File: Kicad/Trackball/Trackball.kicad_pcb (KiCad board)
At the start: 2 copper layers, 305.8 x 154.1 mm, 67 parts, among them J1 Battery, J10 Female, J11 Conn_01x04_Female, J12 Conn_01x04_Female, J13 Female, J14 Conn_01x04_Female, J15 Conn_01x04_Female, J17 Conn_01x04_Female, J18 Conn_01x03_Pin, J19 Conn_01x03_Pin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

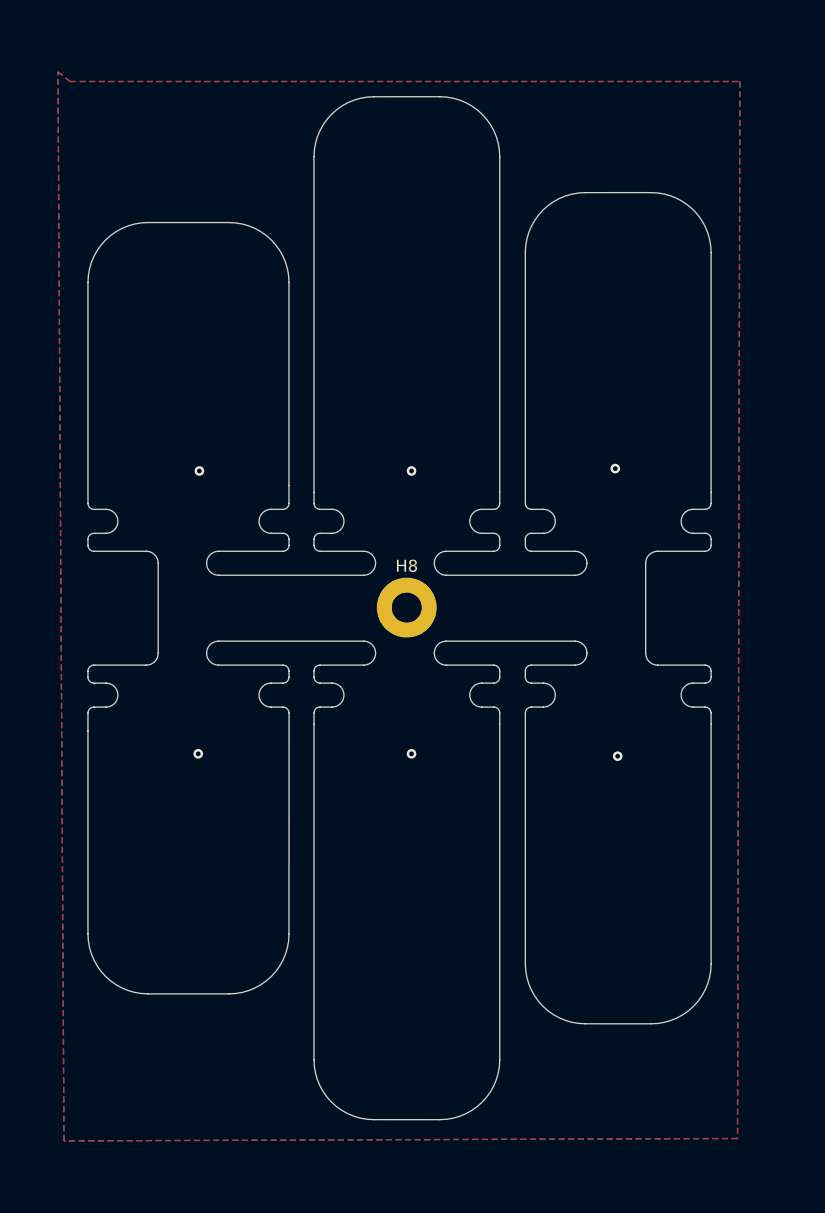
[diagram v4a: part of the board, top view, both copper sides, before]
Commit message: B5: Modified the flaps plate - changed their length as per user feedback. Updated Gerbers for that plate, ordered that plate 20251024.
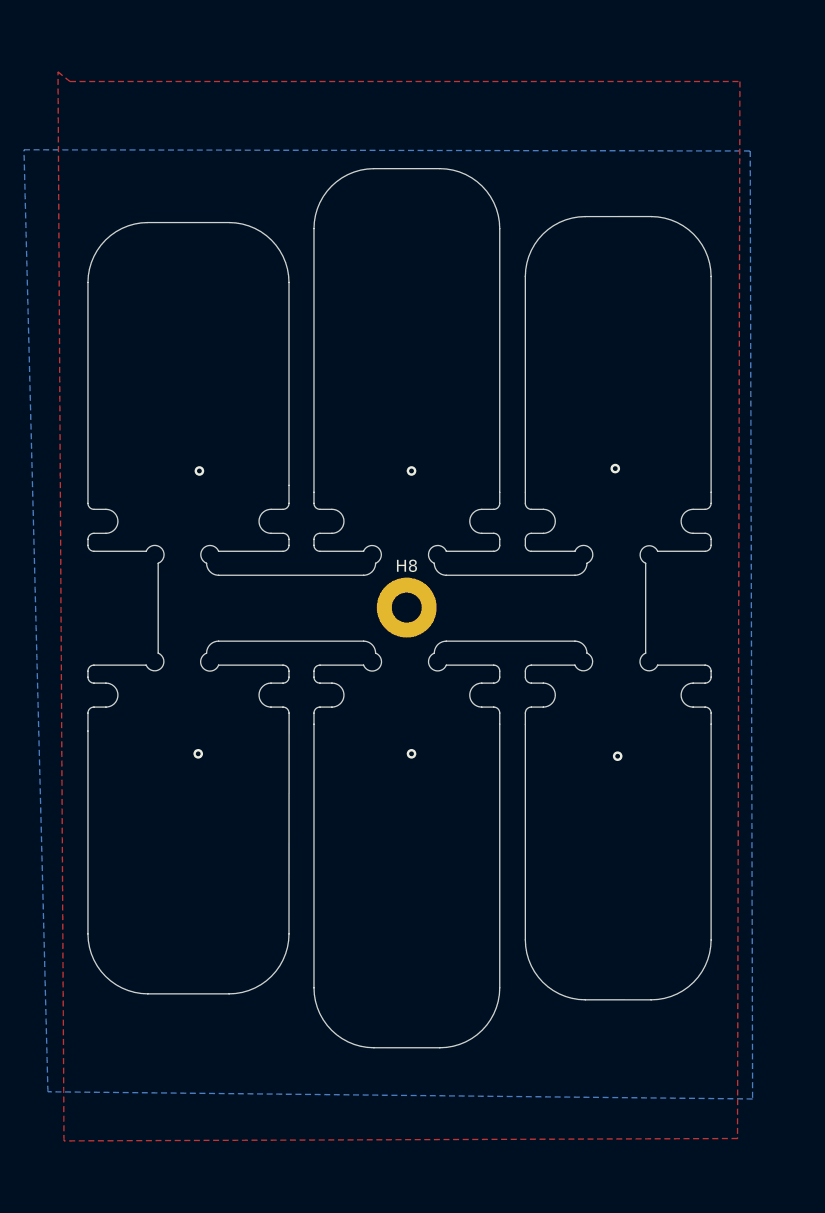
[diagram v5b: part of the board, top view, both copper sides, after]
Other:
- outline, holes or cut-outs redrawn
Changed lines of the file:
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@@
 	)
 	(gr_rect
+		(start -19.95 91.875)
+		(end -15.6 103.325)
+		(stroke
+			(width 0.1)
+			(type solid)
+		)
+		(fill yes)
+		(layer "B.Mask")
+	)
+	(gr_rect
+		(start -37.95 60.05)
+		(end -33.6 71.5)
+		(stroke
+			(width 0.1)
+			(type solid)
+		)
+		(fill yes)
+		(layer "B.Mask")
+	)
+	(gr_rect
+		(start -2.7 60.05)
+		(end 1.65 71.5)
+		(stroke
+			(width 0.1)
+			(type solid)
+		)
+		(fill yes)
+		(layer "B.Mask")
+	)
+	(gr_rect
+		(start -2.7 91.875)
+		(end 1.65 103.325)
+		(stroke
+			(width 0.1)
+			(type solid)
+		)
+		(fill yes)
+		(layer "B.Mask")
+	)
+	(gr_rect
+		(start -20.2 60.05)
+		(end -15.85 71.5)
+		(stroke
+			(width 0.1)
+			(type solid)
+		)
+		(fill yes)
+		(layer "B.Mask")
+	)
+	(gr_rect
+		(start -38.2 91.875)
+		(end -33.85 103.325)
+		(stroke
+			(width 0.1)
+			(type solid)
+		)
+		(fill yes)
+		(layer "B.Mask")
+	)
+	(gr_rect
 		(start 164.775 76.35)
 		(end 170.025 86.85)
@@
 	(gr_arc
 		(start -2.823907 85.4)
-		(mid -3.1168 86.107107)
+		(mid -2.574453 86.649454)
 		(end -3.823907 86.4)
 		(stroke
@@
 	)
 	(gr_arc
-		(start -10.1 119.32842)
-		(mid -11.565025 122.864512)
-		(end -15.10158 124.32842)
+		(start -10.1 113.32842)
+		(mid -11.565025 116.864512)
+		(end -15.10158 118.32842)
 		(stroke
 			(width 0.05)
@@
 	(gr_arc
 		(start -38.6 85.4)
-		(mid -38.892893 86.107107)
+		(mid -38.35 86.65)
 		(end -39.6 86.4)
 		(stroke
@@
 	)
 	(gr_line
-		(start 7.536092 111.32842)
+		(start 7.536092 109.32842)
 		(end 7.536092 91.325102)
 		(stroke
@@
 	)
 	(gr_arc
-		(start -25.6 43.973318)
-		(mid -24.136092 40.438343)
-		(end -20.60158 38.973318)
+		(start -25.6 49.973318)
+		(mid -24.136092 46.438343)
+		(end -20.60158 44.973318)
 		(stroke
 			(width 0.05)
@@
 	)
 	(gr_line
-		(start -2.965488 116.326682)
-		(end 2.534512 116.32842)
+		(start -2.965488 114.326682)
+		(end 2.534512 114.32842)
 		(stroke
 			(width 0.05)
@@
 	)
 	(gr_line
-		(start -25.6 119.326682)
+		(start -25.6 113.326681)
 		(end -25.6 91.325102)
 		(stroke
@@
 	(gr_arc
 		(start -20.459999 85.4)
-		(mid -20.752892 86.107107)
+		(mid -20.192499 86.6675)
 		(end -21.459999 86.4)
 		(stroke
@@
 	(gr_arc
 		(start -21.46 76.9)
-		(mid -20.752893 77.192893)
+		(mid -20.205 76.645)
 		(end -20.46 77.9)
 		(stroke
@@
 	)
 	(gr_arc
-		(start -15.10158 38.97158)
-		(mid -11.565025 40.435487)
-		(end -10.1 43.97158)
+		(start -15.10158 44.97158)
+		(mid -11.565025 46.435487)
+		(end -10.1 49.97158)
 		(stroke
 			(width 0.05)
@@
 	(gr_arc
 		(start -33.559999 86.4)
-		(mid -34.267106 86.107107)
+		(mid -34.83 86.670001)
 		(end -34.559999 85.4)
 		(stroke
@@
 	)
 	(gr_arc
-		(start 7.536092 111.32842)
-		(mid 6.071067 114.864512)
-		(end 2.534512 116.32842)
+		(start 7.536092 109.32842)
+		(mid 6.071067 112.864512)
+		(end 2.534512 114.32842)
 		(stroke
 			(width 0.05)
@@
 	)
 	(gr_line
-		(start -20.60158 38.973318)
-		(end -15.10158 38.97158)
+		(start -20.60158 44.973318)
+		(end -15.10158 44.97158)
 		(stroke
 			(width 0.05)
@@
 	)
 	(gr_line
-		(start -10.1 43.97158)
+		(start -10.1 49.97158)
 		(end -10.1 71.974898)
 		(stroke
@@
 	)
 	(gr_line
-		(start 7.536092 51.97158)
+		(start 7.536092 53.97158)
 		(end 7.536092 71.974898)
 		(stroke
@@
 	)
 	(gr_line
-		(start -7.963908 111.326682)
+		(start -7.963908 109.326681)
 		(end -7.963908 91.325102)
 		(stroke
@@
 	(gr_arc
 		(start -39.6 76.9)
-		(mid -38.892893 77.192893)
+		(mid -38.3375 76.6375)
 		(end -38.6 77.9)
 		(stroke
@@
 	)
 	(gr_arc
-		(start 2.534512 46.97158)
-		(mid 6.071067 48.435487)
-		(end 7.536092 51.97158)
+		(start 2.534512 48.97158)
+		(mid 6.071067 50.435487)
+		(end 7.536092 53.97158)
 		(stroke
 			(width 0.05)
@@
 	)
 	(gr_line
-		(start -7.963908 51.973318)
+		(start -7.963908 53.973318)
 		(end -7.963908 71.974898)
 		(stroke
@@
 	)
 	(gr_line
-		(start -20.60158 124.326682)
-		(end -15.10158 124.32842)
+		(start -20.60158 118.326682)
+		(end -15.10158 118.32842)
 		(stroke
 			(width 0.05)
@@
 	)
 	(gr_arc
-		(start -20.60158 124.326682)
-		(mid -24.136092 122.861657)
-		(end -25.6 119.326682)
+		(start -20.60158 118.326682)
+		(mid -24.136092 116.861657)
+		(end -25.6 113.326682)
 		(stroke
 			(width 0.05)
@@
 	)
 	(gr_line
-		(start -2.965488 46.973318)
-		(end 2.534512 46.97158)
+		(start -2.965488 48.973318)
+		(end 2.534512 48.97158)
 		(stroke
 			(width 0.05)
@@
 	)
 	(gr_arc
-		(start -2.965488 116.326682)
-		(mid -6.5 114.861657)
-		(end -7.963908 111.326682)
+		(start -2.965488 114.326682)
+		(mid -6.5 112.861657)
+		(end -7.963908 109.326682)
 		(stroke
 			(width 0.05)
@@
 	(gr_arc
 		(start 3.076093 86.4)
-		(mid 2.368986 86.107107)
+		(mid 1.825546 86.650547)
 		(end 2.076093 85.4)
 		(stroke
@@
 	)
 	(gr_line
-		(start -25.6 43.973318)
+		(start -25.6 49.973319)
 		(end -25.6 71.974898)
 		(stroke
@@
 	)
 	(gr_line
-		(start -10.1 119.32842)
+		(start -10.1 113.32842)
 		(end -10.1 91.325102)
 		(stroke
@@
 	(gr_arc
 		(start -14.559999 86.4)
-		(mid -15.267106 86.107107)
+		(mid -15.8175 86.657501)
 		(end -15.559999 85.4)
 		(stroke
@@
 	(gr_arc
 		(start -15.56 77.9)
-		(mid -15.267107 77.192893)
+		(mid -15.8175 76.6425)
 		(end -14.56 76.9)
 		(stroke
@@
 	)
 	(gr_arc
-		(start -7.963908 51.973318)
-		(mid -6.5 48.438343)
-		(end -2.965488 46.973318)
+		(start -7.963908 53.973318)
+		(mid -6.5 50.438343)
+		(end -2.965488 48.973318)
 		(stroke
 			(width 0.05)
@@
 	(gr_arc
 		(start -34.56 77.9)
-		(mid -34.267107 77.192893)
+		(mid -34.8175 76.6425)
 		(end -33.56 76.9)
 		(stroke
@@
 	(gr_arc
 		(start -3.823908 76.9)
-		(mid -3.116801 77.192893)
+		(mid -2.561954 76.638046)
 		(end -2.823908 77.9)
 		(stroke
@@
 	(gr_arc
 		(start 2.076092 77.9)
-		(mid 2.368985 77.192893)
+		(mid 1.838046 76.661954)
 		(end 3.076092 76.9)
 		(stroke
@@
 	)
 	(gr_text "L3"
-		(at -0.8 98.1 180)
+		(at -1.575 105.1 180)
 		(layer "B.SilkS")
 		(effects
@@
 	)
 	(gr_text "L1"
-		(at -36.3 99 180)
+		(at -37.425 105.1 180)
 		(layer "B.SilkS")
 		(effects
@@
 	)
 	(gr_text "R2"
-		(at -16.7 61.9 0)
+		(at -16.7 58 0)
 		(layer "B.SilkS")
 		(effects
@@
 	)
 	(gr_text "R1"
-		(at -33.9 62.2 0)
+		(at -33.9 58 0)
 		(layer "B.SilkS")
 		(effects
@@
 	)
 	(gr_text "R3"
-		(at 1.1 62 0)
+		(at 1.1 58 0)
 		(layer "B.SilkS")
 		(effects
@@
 	)
 	(gr_text "L2"
-		(at -18.8 99 180)
+		(at -18.975 105.1 180)
 		(layer "B.SilkS")
 		(effects
@@
 	)
 	(zone
+		(net 68)
+		(net_name "GND_F")
+		(layer "F.Cu")
+		(hatch edge 0.5)
+		(priority 5)
+		(connect_pads
+			(clearance 0.508)
+		)
+		(min_thickness 0.25)
+		(filled_areas_thickness no)
+		(fill yes
+			(mode hatch)
+			(thermal_gap 0.5)
+			(thermal_bridge_width 0.5)
+			(hatch_thickness 1)
+			(hatch_gap 1.5)
+			(hatch_orientation 45)
+			(hatch_border_algorithm hatch_thickness)
+			(hatch_min_hole_area 0.3)
+		)
+		(polygon
+			(pts
+				(xy -46.96 36.9) (xy -45.96 37.7) (xy 9.94 37.7) (xy 9.74 125.9) (xy -46.46 126.1)
+			)
+		)
+	)
+	(zone
 		(net 1)
 		(net_name "GND")
@@
 		(net 68)
 		(net_name "GND_F")
-		(layers "F.Cu" "B.Cu")
+		(layer "B.Cu")
 		(hatch edge 0.5)
-		(priority 5)
+		(priority 3)
 		(connect_pads
 			(clearance 0.508)
@@
 		(filled_areas_thickness no)
 		(fill yes
-			(mode hatch)
 			(thermal_gap 0.5)
 			(thermal_bridge_width 0.5)
-			(hatch_thickness 1)
-			(hatch_gap 1.5)
-			(hatch_orientation 45)
-			(hatch_border_algorithm hatch_thickness)
-			(hatch_min_hole_area 0.3)
 		)
 		(polygon
 			(pts
-				(xy -46.96 36.9) (xy -45.96 37.7) (xy 9.94 37.7) (xy 9.74 125.9) (xy -46.46 126.1)
+				(xy -49.8 43.4) (xy 10.8 43.5) (xy 11 122.6) (xy -47.8 122)
 			)
 		)

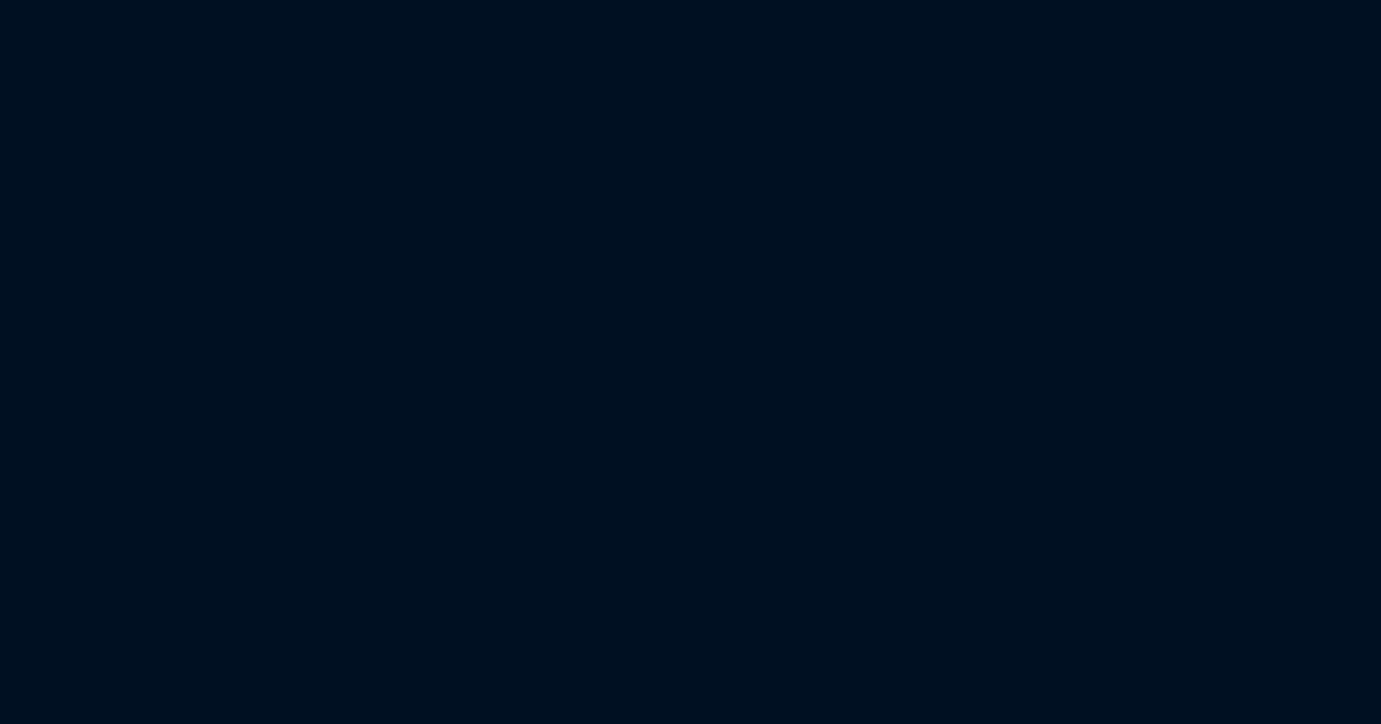
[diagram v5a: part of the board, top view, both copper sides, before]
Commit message: B5: Added a 3D-printed palm support piece.
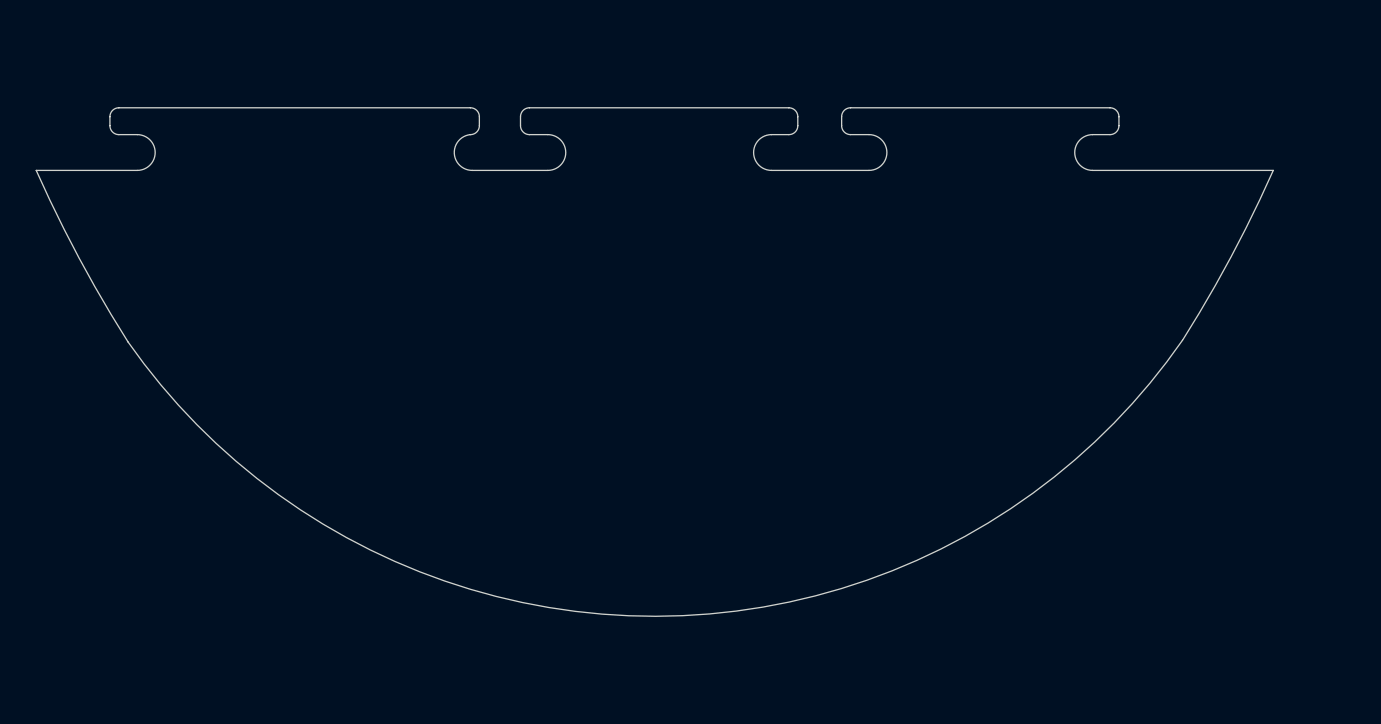
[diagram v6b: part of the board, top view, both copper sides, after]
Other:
- board size 305.8 x 154.1 mm -> 391 x 154.1 mm

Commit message: B5: Rev.1 changes.
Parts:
- removed H2, H3: MountingHole_Pad, MountingHole:MountingHole_2.5mm_Pad
- moved JP2 8.00 mm to (217.4, 44.5)
- moved JP5 8.00 mm to (217.2, 118.7)
- moved MX2 8.00 mm to (220.4, 49.6)
- moved MX5 8.00 mm to (220.4, 113.6)
- moved JP1 2.00 mm to (116.2, 44.8)
- moved JP4 2.00 mm to (115.9, 118.5)
- moved MX1 2.00 mm to (112.7, 49.9)
- moved MX4 2.00 mm to (112.7, 113.4)
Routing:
- net Net-(J13-Pin_2): track 29.5 -> 22.7 mm
- net Net-(J10-Pin_2): track 29.7 -> 23.1 mm
- net Button4: track 66.1 -> 64.1 mm
- net Button1: track 46.7 -> 44.7 mm
- net GND: track 4.10 -> 2.37 mm
- net Net-(JP2-A): track 5.01 -> 4.19 mm
- net Net-(JP5-A): track 5.13 -> 4.60 mm
- net Net-(JP5-B): track 5.13 -> 4.60 mm
- added copper zone on B.Cu, net (none)
- removed copper zone on B.Cu, net GNDA
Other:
- outline, holes or cut-outs redrawn
- board text added: "u/ak66666 2026-05-03 ThumbsUp! Trackball v5 rev.1"
- board text removed: "u/ak66666 ThumbsUp! Trackball v5 2025-09-26"
